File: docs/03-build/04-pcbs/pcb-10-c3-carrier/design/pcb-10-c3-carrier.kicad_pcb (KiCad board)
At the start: 2 copper layers, 70 x 49.5 mm, 0 parts

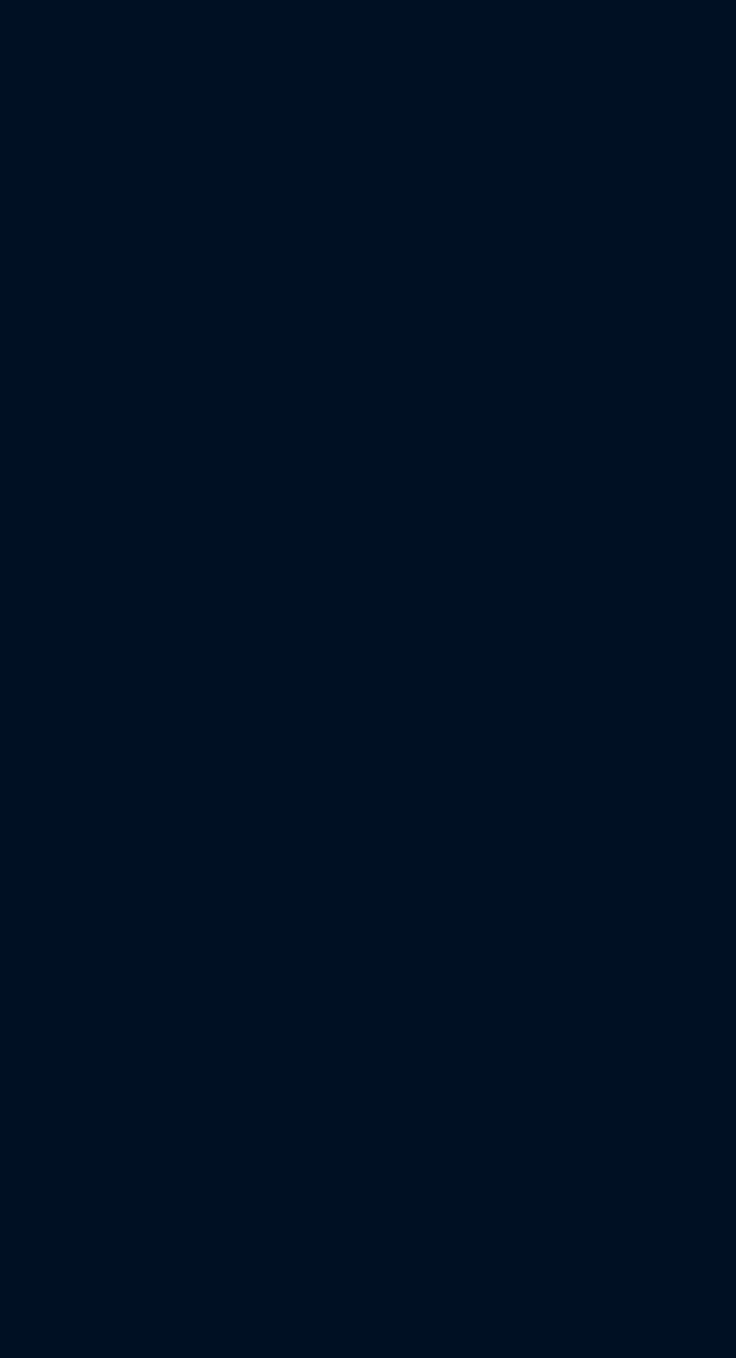
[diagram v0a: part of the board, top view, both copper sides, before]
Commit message: build(pcbs): PCB-10 placement, DRC clean; J10-2 reordered, GPIO map v0.3 for routing (lesson 4, part 1)
All 90 footprints placed through KiPy on the proved connector origins;
DRC: no courtyard, edge or parity errors (53 cosmetic rotated-footprint
library mismatches, the PCB-15 trap). J10-2 takes U2's own pin order so
the RS-422 pairs run straight (PCB-09 and 05-harness updated); the GPIO
map is reassigned (v0.3) so each pin sits next to the connector it feeds.
Schematic regenerated, ERC 0/0, board pad nets updated to match.

Co-Authored-By: Claude Opus 5.5 <noreply@anthropic.com>
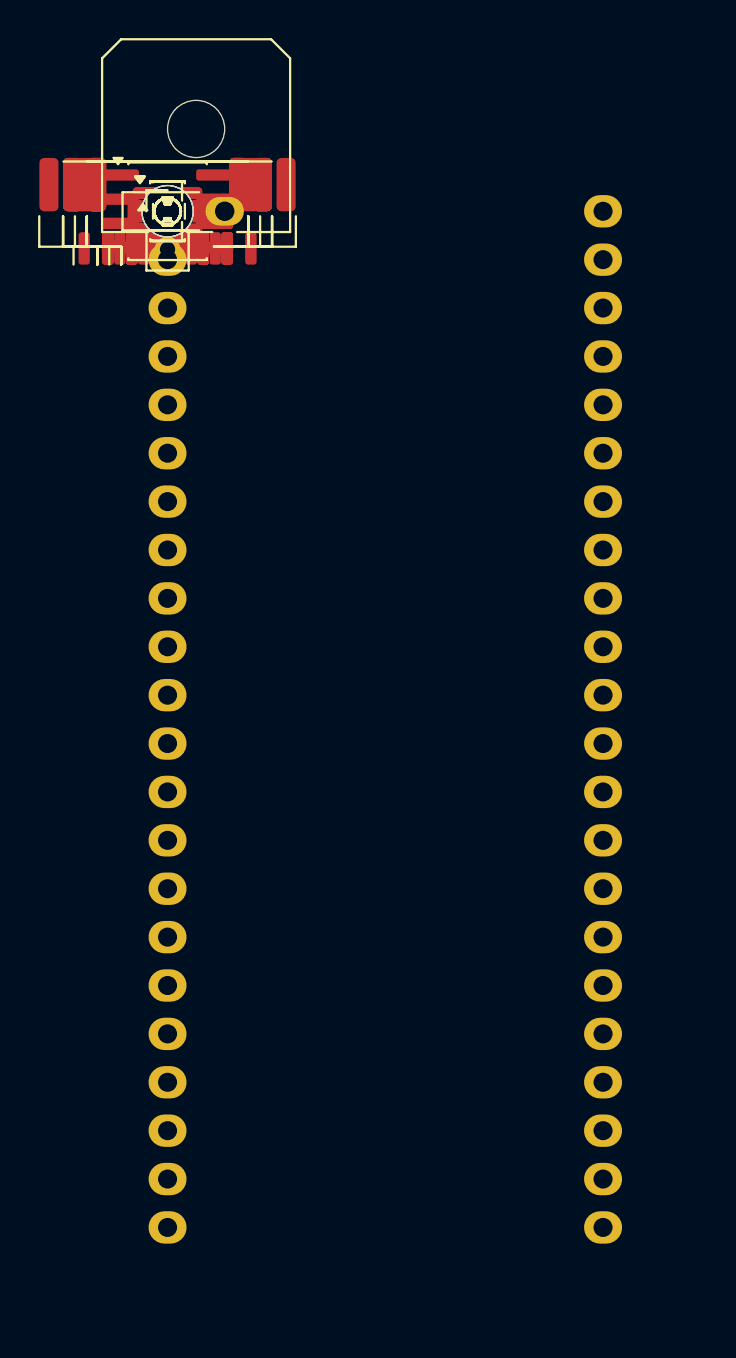
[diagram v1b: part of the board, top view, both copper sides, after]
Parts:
- added C1, C10, C3: 10u X5R 10V, Capacitor_SMD:C_0805_2012Metric, F.Cu at (0.00, 0.00)
- added C11, C2, C4, C5, C6, C7, C8: 100n X7R 16V, Capacitor_SMD:C_0402_1005Metric, F.Cu at (0.00, 0.00)
- added C12, C9: 1n X7R 50V, Capacitor_SMD:C_0402_1005Metric, F.Cu at (0.00, 0.00)
- added D1: B5819W, Diode_SMD:D_SOD-123, F.Cu at (0.00, 0.00)
- added H1, H2: M2.5 (lower screws, D-068 A), MountingHole:MountingHole_2.7mm_M2.5, F.Cu at (0.00, 0.00)
- added J1: J10-1 +5 V (W11), pcb10:Molex_Micro-Fit_3.0_43650-0200_1x02_P3.00mm_Horizontal, F.Cu at (0.00, 0.00)
- added J10: J10-10 rear TCRT (W36), Connector_JST:JST_GH_BM04B-GHS-TBT_1x04-1MP_P1.25mm_Vertical, F.Cu at (0.00, 0.00)
- added J12: J10-12 readiness (W39, PCB-03 J3-9), Connector_JST:JST_GH_BM04B-GHS-TBT_1x04-1MP_P1.25mm_Vertical, F.Cu at (0.00, 0.00)
- added J2: J10-2 base link (W25), Connector_JST:JST_GH_BM06B-GHS-TBT_1x06-1MP_P1.25mm_Vertical, F.Cu at (0.00, 0.00)
- added J3: J10-3 encoder L (W30), Connector_JST:JST_GH_BM04B-GHS-TBT_1x04-1MP_P1.25mm_Vertical, F.Cu at (0.00, 0.00)
- added J4: J10-4 encoder R (W31), Connector_JST:JST_GH_BM04B-GHS-TBT_1x04-1MP_P1.25mm_Vertical, F.Cu at (0.00, 0.00)
- added J5: J10-5 left DRV8833 (W32), Connector_JST:JST_GH_BM06B-GHS-TBT_1x06-1MP_P1.25mm_Vertical, F.Cu at (0.00, 0.00)
- added J6: J10-6 right DRV8833 (W33), Connector_JST:JST_GH_BM06B-GHS-TBT_1x06-1MP_P1.25mm_Vertical, F.Cu at (0.00, 0.00)
- added J7: J10-7 IMU PCB-07 (W29), Connector_JST:JST_GH_BM08B-GHS-TBT_1x08-1MP_P1.25mm_Vertical, F.Cu at (0.00, 0.00)
- added J8: J10-8 nose (W34), Connector_JST:JST_GH_BM05B-GHS-TBT_1x05-1MP_P1.25mm_Vertical, F.Cu at (0.00, 0.00)
- added JP1: JP_SVC (shunt = watchdog off, READY low), Connector_PinHeader_2.00mm:PinHeader_1x02_P2.00mm_Vertical, F.Cu at (0.00, 0.00)
- added Q1: AO3400A, Package_TO_SOT_SMD:SOT-23, F.Cu at (0.00, 0.00)
- added R1, R15, R2, R3, R33, R38, R4, R5: 10k, Resistor_SMD:R_0402_1005Metric, F.Cu at (0.00, 0.00)
- added R10, R16, R32, R37, R41, R42, R6, R9: 1k, Resistor_SMD:R_0402_1005Metric, F.Cu at (0.00, 0.00)
- added R11, R12, R13, R14, R20, R21, R22, R23: 100, Resistor_SMD:R_0402_1005Metric, F.Cu at (0.00, 0.00)
- added R17: 120, Resistor_SMD:R_0402_1005Metric, F.Cu at (0.00, 0.00)
- added R18, R19: DNP 560, Resistor_SMD:R_0402_1005Metric, F.Cu at (0.00, 0.00)
- added R24, R25, R26, R27: DNP 10k, Resistor_SMD:R_0402_1005Metric, F.Cu at (0.00, 0.00)
- added R28, R29, R30, R31: 33, Resistor_SMD:R_0402_1005Metric, F.Cu at (0.00, 0.00)
- added R34: 100, Resistor_SMD:R_0603_1608Metric, F.Cu at (0.00, 0.00)
- added R35, R43, R7, R8: 100k, Resistor_SMD:R_0402_1005Metric, F.Cu at (0.00, 0.00)
- added R36: 10k, Resistor_SMD:R_0603_1608Metric, F.Cu at (0.00, 0.00)
- added R39: 22k, Resistor_SMD:R_0402_1005Metric, F.Cu at (0.00, 0.00)
- added R40: 1M, Resistor_SMD:R_0402_1005Metric, F.Cu at (0.00, 0.00)
- added TP1: +5V_IN, TestPoint:TestPoint_Pad_D1.0mm, F.Cu at (0.00, 0.00)
- added TP10: WDO, TestPoint:TestPoint_Pad_D1.0mm, F.Cu at (0.00, 0.00)
- added TP11: READY, TestPoint:TestPoint_Pad_D1.0mm, F.Cu at (0.00, 0.00)
- added TP12: SLP, TestPoint:TestPoint_Pad_D1.0mm, F.Cu at (0.00, 0.00)
- added TP13: FLT, TestPoint:TestPoint_Pad_D1.0mm, F.Cu at (0.00, 0.00)
- added TP14: MR, TestPoint:TestPoint_Pad_D1.0mm, F.Cu at (0.00, 0.00)
- added TP15: WD_EN, TestPoint:TestPoint_Pad_D1.0mm, F.Cu at (0.00, 0.00)
- added TP2: +5V_DK, TestPoint:TestPoint_Pad_D1.0mm, F.Cu at (0.00, 0.00)
- added TP3: +3V3, TestPoint:TestPoint_Pad_D1.0mm, F.Cu at (0.00, 0.00)
- added TP4: GND, TestPoint:TestPoint_Pad_D1.0mm, F.Cu at (0.00, 0.00)
- added TP5: C3TX_P, TestPoint:TestPoint_Pad_D1.0mm, F.Cu at (0.00, 0.00)
- added TP6: C3TX_N, TestPoint:TestPoint_Pad_D1.0mm, F.Cu at (0.00, 0.00)
- added TP7: C0TX_P, TestPoint:TestPoint_Pad_D1.0mm, F.Cu at (0.00, 0.00)
- added TP8: C0TX_N, TestPoint:TestPoint_Pad_D1.0mm, F.Cu at (0.00, 0.00)
- added TP9: WDI, TestPoint:TestPoint_Pad_D1.0mm, F.Cu at (0.00, 0.00)
- added U1: ESP32-S3-DevKitC-1-N8, pcb10:ESP32-S3-DevKitC-1_v1.1_1.0mm, F.Cu at (0.00, 0.00)
- added U2: THVD1451DR, Package_SO:SOIC-8_3.9x4.9mm_P1.27mm, F.Cu at (0.00, 0.00)
- added U3: TPS3436CCCBGDDFRQ1, pcb10:Texas_DDF0008A_SOT-8_1.6x2.9mm_P0.65mm, F.Cu at (0.00, 0.00)
- added U4: 74LVC1G08, Package_TO_SOT_SMD:SOT-23-5, F.Cu at (0.00, 0.00)
- added U5: 74LVC1G11, Package_TO_SOT_SMD:SOT-23-6, F.Cu at (0.00, 0.00)
